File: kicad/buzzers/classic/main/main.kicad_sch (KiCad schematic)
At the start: 0 parts

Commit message: feat: Added main Classic buzzer board; now basically just waiting on XLR5 and HW-0519 footprints; also need to see if I need a separate earth for the HW-0519s on the buzzer boards
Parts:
- added C1: 100n, symbol Device:C
- added J1, J2: Conn_01x05, symbol Connector_Generic:Conn_01x05
- added J3: Conn_01x04, symbol Connector_Generic:Conn_01x04
- added R1: 4.7k, symbol Device:R
- added U1: ATtiny412-SS, Package_SO:SOIC-8_3.9x4.9mm_P1.27mm, symbol MCU_Microchip_ATtiny:ATtiny412-SS
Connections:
- new net: R1.2, U1.6 (~{RESET}/PA0)
- new net +3V3: C1.1, J1.5 (Pin_5), J2.5 (Pin_5), J3.4 (Pin_4), R1.1, U1.1 (VCC)
- new net GND: C1.2, J1.1 (Pin_1), J2.1 (Pin_1), J3.1 (Pin_1), U1.8 (GND)
- new net HW_SERIAL_TX: U1.3 (PA7)
- new net LED_OUT: J3.3 (Pin_3), U1.5 (PA2)
- new net RS485_A: J1.4 (Pin_4), J2.4 (Pin_4)
- new net RS485_B: J1.3 (Pin_3), J2.3 (Pin_3)
- new net SERIAL_BB_RX: J1.2 (Pin_2), U1.2 (PA6)
- new net SERIAL_BB_TX: J2.2 (Pin_2), U1.7 (PA3)
- new net SW_IN: J3.2 (Pin_2), U1.4 (PA1)
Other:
- note added: "Connector to XLR5 daughterboard (from prev. buzzer/control unit)"
- note added: "Connector to XLR5 daughterboard (to next buzzer)"
- note added: "Connector to button/LED daughterboard"
- note added: "HW-0519 (RS485) TODO"

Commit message: feat: Added connector schematics and fixed some other connectors in other schematics
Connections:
- net RS485_A: now also J1.2 (Pin_2); no longer J1.4 (Pin_4)
- net SERIAL_BB_RX: now also J1.4 (Pin_4); no longer J1.2 (Pin_2)
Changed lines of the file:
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@@
-		)
-	)
-	(label "RS485_A"
-		(at 25.4 38.1 270)
-		(effects
-			(font
-				(size 1.27 1.27)
-			)
-			(justify right bottom)
-		)
-	)
-	(label "SERIAL_BB_RX"
-		(at 30.48 38.1 270)
-		(effects
-			(font
-				(size 1.27 1.27)
-			)
-			(justify right bottom)
 		)
 	)
@@
 		)
 	)
+	(label "RS485_A"
+		(at 30.48 38.1 270)
+		(effects
+			(font
+				(size 1.27 1.27)
+			)
+			(justify right bottom)
+		)
+	)
+	(label "SERIAL_BB_RX"
+		(at 25.4 38.1 270)
+		(effects
+			(font
+				(size 1.27 1.27)
+			)
+			(justify right bottom)
+		)
+	)

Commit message: Added ESD protection for USB/RS485, not for serial lines yet; harmonised XLR pin numbers between boards
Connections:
- net RS485_A: now also J2.2 (Pin_2); no longer J2.4 (Pin_4)
- net SERIAL_BB_TX: now also J2.4 (Pin_4); no longer J2.2 (Pin_2)
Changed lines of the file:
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@@
-	(wire
-		(pts
-			(xy 53.34 25.4) (xy 53.34 29.21)
-		)
-		(stroke
-			(width 0)
-			(type default)
-		)
-	)
 	(wire
 		(pts
@@
 		)
 	)
-	(label "SERIAL_BB_TX"
-		(at 58.42 29.21 90)
+	(label "RS485_B"
+		(at 55.88 29.21 90)
 		(effects
 			(font
@@
 		)
 	)
+	(label "RS485_A"
+		(at 58.42 29.21 90)
+		(effects
+			(font
+				(size 1.27 1.27)
+			)
+			(justify left bottom)
+		)
+	)
 	(label "LED_OUT"
 		(at 191.77 24.13 90)
@@
 		)
 	)
-	(label "RS485_A"
-		(at 53.34 25.4 90)
+	(label "SERIAL_BB_TX"
+		(at 53.34 29.21 90)
 		(effects
 			(font
@@
 		)
 	)
-	(label "RS485_B"
-		(at 55.88 29.21 90)
-		(effects
-			(font
-				(size 1.27 1.27)
-			)
-			(justify left bottom)
-		)
-	)

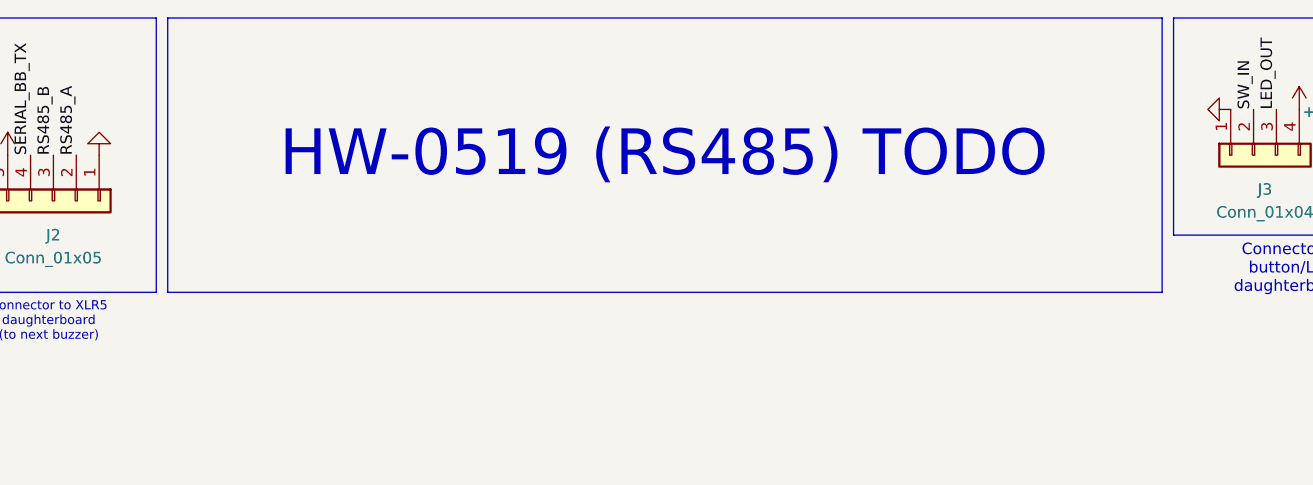
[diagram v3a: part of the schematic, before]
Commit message: feat: Should be able to footprint and route some prototype boards to see if I'm not totally off-base here
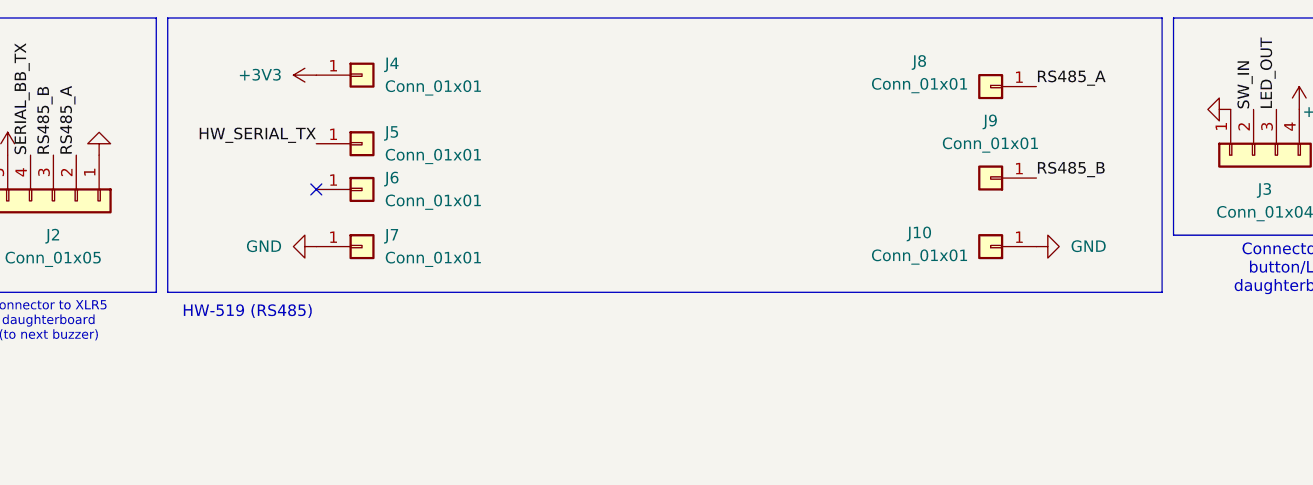
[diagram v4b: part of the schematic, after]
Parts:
- added J10, J4, J5, J6, J7, J8, J9: Conn_01x01, symbol Connector_Generic:Conn_01x01
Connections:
- net +3V3: now also J4.1 (Pin_1)
- net GND: now also J10.1 (Pin_1), J7.1 (Pin_1)
- net HW_SERIAL_TX: now also J5.1 (Pin_1)
- net RS485_A: now also J8.1 (Pin_1)
- net RS485_B: now also J9.1 (Pin_1)
- no-connect marks 0 -> 1
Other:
- note added: "HW-519 (RS485)"
- note removed: "HW-0519 (RS485) TODO"
